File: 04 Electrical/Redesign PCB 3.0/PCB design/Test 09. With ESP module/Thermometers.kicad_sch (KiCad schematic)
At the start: 5 parts, among them U6 DS18S20, U7 DS18S20, U8 DS18S20, U9 DS18S20

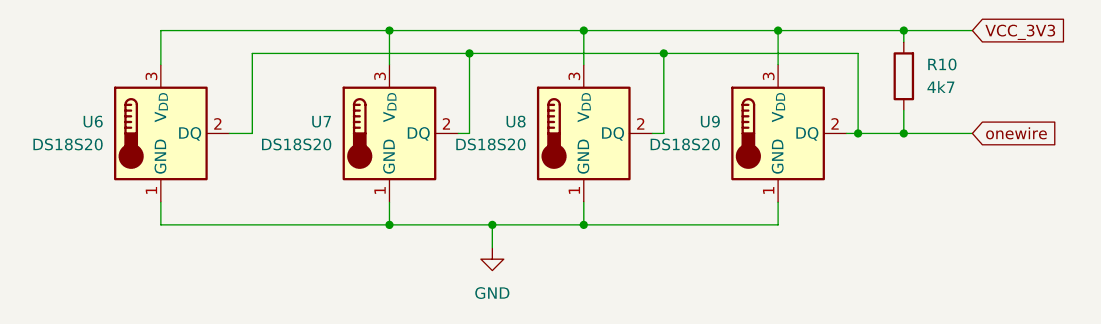
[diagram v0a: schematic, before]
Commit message: Logo added to PCB
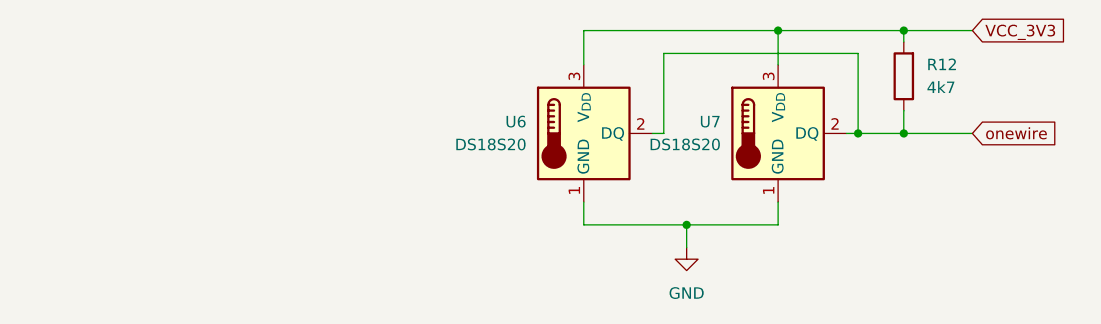
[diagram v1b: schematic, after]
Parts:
- removed U6, U7: DS18S20, Package_TO_SOT_THT:TO-92L_HandSolder, symbol Sensor_Temperature:DS18S20
- renumbered R10 to R12, U8 to U6, U9 to U7

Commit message: As ordered at JLCPCB
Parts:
- U6, U7: now not fitted
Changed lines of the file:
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@@
 			)
 		)
-		(property "Description" "Resistor"
+		(property "Description" "100mW Thick Film Resistors 75V ±100ppm/℃ ±1% 4.7kΩ 0603 Chip Resistor - Surface Mount ROHS"
 			(at 195.58 86.36 0)
 			(effects
@@
 		)
 		(property "LCSC Part # " "C23162"
+			(at 195.58 86.36 0)
+			(effects
+				(font
+					(size 1.27 1.27)
+				)
+				(hide yes)
+			)
+		)
+		(property "Comment" ""
 			(at 195.58 86.36 0)
 			(effects
@@
 		(in_bom no)
 		(on_board yes)
-		(dnp no)
+		(dnp yes)
 		(fields_autoplaced yes)
 		(property "Reference" "U6"
@@
 			)
 		)
-		(property "Field7" ""
+		(property "Comment" ""
 			(at 160.02 92.71 0)
 			(effects
@@
 		(dnp no)
 		(fields_autoplaced yes)
-		(property "Reference" "#PWR030"
+		(property "Reference" "#PWR028"
 			(at 171.45 111.76 0)
 			(effects
@@
 			(project ""
 				(path "/dee7d3c3-6abb-4cb3-8df4-3e3e37989a04/1ee783e5-877a-4e23-8a1c-34a8f840b01c"
-					(reference "#PWR030")
+					(reference "#PWR028")
 					(unit 1)
 				)
@@
 		(in_bom no)
 		(on_board yes)
-		(dnp no)
+		(dnp yes)
 		(fields_autoplaced yes)
 		(property "Reference" "U7"
@@
 			)
 		)
-		(property "Field7" ""
+		(property "Comment" ""
 			(at 181.61 92.71 0)
 			(effects
